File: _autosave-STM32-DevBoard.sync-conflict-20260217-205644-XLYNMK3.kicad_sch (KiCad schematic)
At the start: 55 parts, among them J1 I2C Bus 1, J2 Serial Debugger, J3 USART1, J4 12402012E212A, J5 PJ-002A, Q1 AO3401A, SW1 SW_SPDT, U1 STM32F103C8T6, U2 TPS563209DDCR, U3 USBLC6-2SC6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

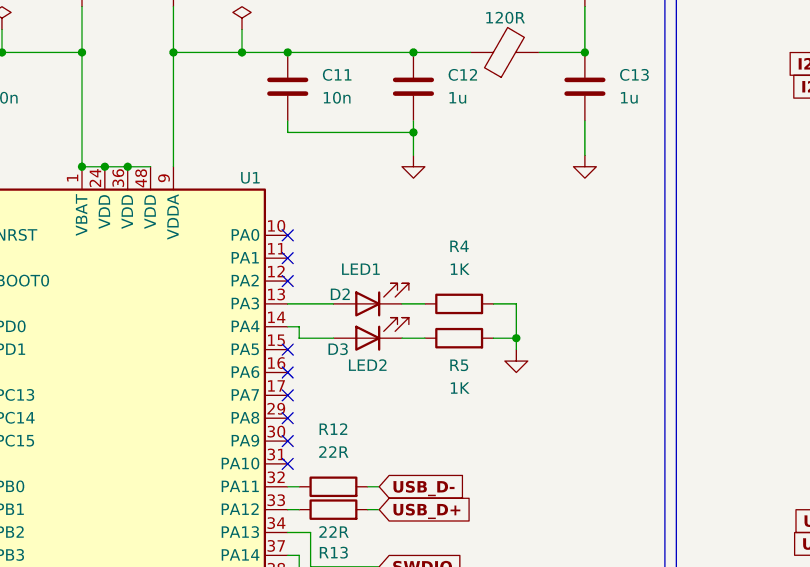
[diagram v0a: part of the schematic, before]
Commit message: Schematic complete, preliminary pcb layout done
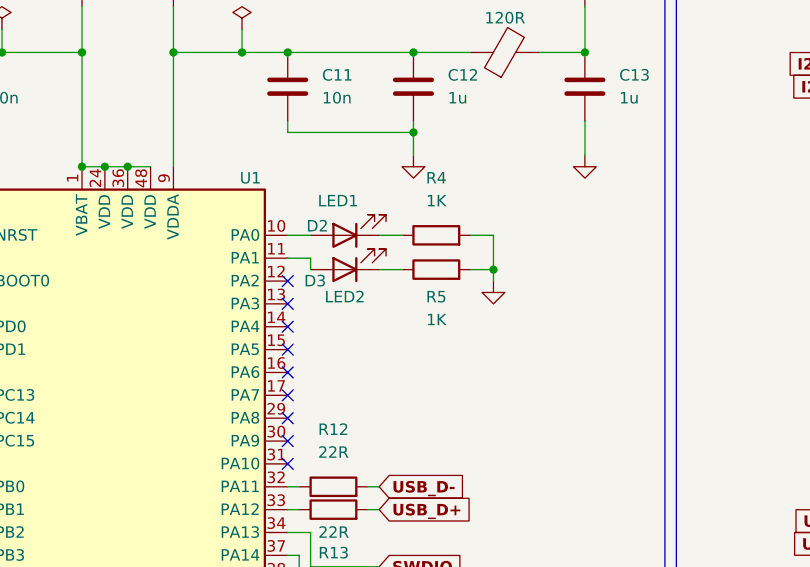
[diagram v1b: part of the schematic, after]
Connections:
- net at D3.2 (A): now also U1.11 (PA1); no longer U1.14 (PA4)
- net at U1.10 (PA0): now also D2.2 (A)
- net at U1.13 (PA3): no longer D2.2 (A)
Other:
- moved on the sheet: D2, D3, R4, R5
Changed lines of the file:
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@@
 	)
 	(junction
-		(at 133.35 120.65)
+		(at 130.81 113.03)
 		(diameter 0)
 		(color 0 0 0 0)
@@
 	)
 	(no_connect
-		(at 107.95 109.22)
+		(at 107.95 119.38)
 	)
 	(no_connect
@@
 	)
 	(no_connect
+		(at 107.95 116.84)
+	)
+	(no_connect
 		(at 72.39 129.54)
 	)
@@
 		(at 72.39 167.64)
 	)
-	(no_connect
-		(at 107.95 111.76)
-	)
 	(wire
 		(pts
@@
 	(wire
 		(pts
-			(xy 109.22 119.38) (xy 109.22 120.65)
+			(xy 46.99 96.52) (xy 46.99 97.79)
 		)
 		(stroke
@@
 	(wire
 		(pts
-			(xy 46.99 96.52) (xy 46.99 97.79)
+			(xy 215.9 132.08) (xy 218.44 132.08)
 		)
 		(stroke
@@
 	(wire
 		(pts
-			(xy 215.9 132.08) (xy 218.44 132.08)
+			(xy 128.27 109.22) (xy 130.81 109.22)
 		)
 		(stroke
@@
 	(wire
 		(pts
-			(xy 130.81 116.84) (xy 133.35 116.84)
+			(xy 110.49 111.76) (xy 110.49 113.03)
 		)
 		(stroke
@@
 	(wire
 		(pts
-			(xy 133.35 116.84) (xy 133.35 120.65)
+			(xy 130.81 109.22) (xy 130.81 113.03)
 		)
 		(stroke
@@
 	(wire
 		(pts
-			(xy 130.81 120.65) (xy 133.35 120.65)
+			(xy 128.27 113.03) (xy 130.81 113.03)
 		)
 		(stroke
@@
 	(wire
 		(pts
-			(xy 109.22 120.65) (xy 113.03 120.65)
+			(xy 107.95 111.76) (xy 110.49 111.76)
 		)
 		(stroke
@@
 	(wire
 		(pts
+			(xy 107.95 109.22) (xy 110.49 109.22)
+		)
+		(stroke
+			(width 0)
+			(type default)
+		)
+	)
+	(wire
+		(pts
 			(xy 182.88 138.43) (xy 177.8 138.43)
 		)
@@
 	(wire
 		(pts
-			(xy 107.95 116.84) (xy 113.03 116.84)
-		)
-		(stroke
-			(width 0)
-			(type default)
-		)
-	)
-	(wire
-		(pts
 			(xy 110.49 146.05) (xy 110.49 142.24)
 		)
@@
 	(wire
 		(pts
-			(xy 120.65 116.84) (xy 123.19 116.84)
+			(xy 118.11 109.22) (xy 120.65 109.22)
 		)
 		(stroke
@@
 	(wire
 		(pts
-			(xy 107.95 119.38) (xy 109.22 119.38)
-		)
-		(stroke
-			(width 0)
-			(type default)
-		)
-	)
-	(wire
-		(pts
 			(xy 99.06 44.45) (xy 99.06 54.61)
 		)
@@
 	(wire
 		(pts
-			(xy 133.35 120.65) (xy 133.35 121.92)
+			(xy 130.81 113.03) (xy 130.81 114.3)
 		)
 		(stroke
@@
 	(wire
 		(pts
-			(xy 120.65 120.65) (xy 123.19 120.65)
+			(xy 118.11 113.03) (xy 120.65 113.03)
 		)
 		(stroke
@@
 	(symbol
 		(lib_id "Device:R")
-		(at 127 116.84 90)
+		(at 124.46 109.22 90)
 		(unit 1)
 		(exclude_from_sim no)
@@
 		(fields_autoplaced yes)
 		(property "Reference" "R4"
-			(at 127 110.49 90)
+			(at 124.46 102.87 90)
 			(effects
 				(font
@@
 		)
 		(property "Value" "1K"
-			(at 127 113.03 90)
+			(at 124.46 105.41 90)
 			(effects
 				(font
@@
 		)
 		(property "Footprint" "Resistor_SMD:R_0402_1005Metric"
-			(at 127 118.618 90)
+			(at 124.46 110.998 90)
 			(effects
 				(font
@@
 		)
 		(property "Datasheet" "~"
-			(at 127 116.84 0)
+			(at 124.46 109.22 0)
 			(effects
 				(font
@@
 		)
 		(property "Description" "Resistor"
-			(at 127 116.84 0)
+			(at 124.46 109.22 0)
 			(effects
 				(font
@@
 	(symbol
 		(lib_id "power:GND")
-		(at 133.35 121.92 0)
+		(at 130.81 114.3 0)
 		(unit 1)
 		(exclude_from_sim no)
@@
 		(fields_autoplaced yes)
 		(property "Reference" "#PWR015"
-			(at 133.35 128.27 0)
+			(at 130.81 120.65 0)
 			(effects
 				(font
@@
 		)
 		(property "Value" "GND"
-			(at 133.35 127 0)
+			(at 130.81 119.38 0)
 			(effects
 				(font
@@
 		)
 		(property "Footprint" ""
-			(at 133.35 121.92 0)
+			(at 130.81 114.3 0)
 			(effects
 				(font
@@
 		)
 		(property "Datasheet" ""
-			(at 133.35 121.92 0)
+			(at 130.81 114.3 0)
 			(effects
 				(font
@@
 		)
 		(property "Description" "Power symbol creates a global label with name \"GND\" , ground"
-			(at 133.35 121.92 0)
+			(at 130.81 114.3 0)
 			(effects
 				(font
@@
 	(symbol
 		(lib_id "Device:R")
-		(at 127 120.65 90)
+		(at 124.46 113.03 90)
 		(unit 1)
 		(exclude_from_sim no)
@@
 		(dnp no)
 		(property "Reference" "R5"
-			(at 127 123.698 90)
+			(at 124.46 116.078 90)
 			(effects
 				(font
@@
 		)
 		(property "Value" "1K"
-			(at 127 126.238 90)
+			(at 124.46 118.618 90)
 			(effects
 				(font
@@
 		)
 		(property "Footprint" "Resistor_SMD:R_0402_1005Metric"
-			(at 127 122.428 90)
+			(at 124.46 114.808 90)
 			(effects
 				(font
@@
 		)
 		(property "Datasheet" "~"
-			(at 127 120.65 0)
+			(at 124.46 113.03 0)
 			(effects
 				(font
@@
 		)
 		(property "Description" "Resistor"
-			(at 127 120.65 0)
+			(at 124.46 113.03 0)
 			(effects
 				(font
@@
 	(symbol
 		(lib_id "Device:LED")
-		(at 116.84 120.65 180)
+		(at 114.3 113.03 180)
 		(unit 1)
 		(exclude_from_sim no)
@@
 		(dnp no)
 		(property "Reference" "D3"
-			(at 113.538 121.92 0)
+			(at 110.998 114.3 0)
 			(effects
 				(font
@@
 		)
 		(property "Value" "LED2"
-			(at 116.84 123.698 0)
+			(at 114.3 116.078 0)
 			(effects
 				(font
@@
 		)
 		(property "Footprint" "LED_SMD:LED_0603_1608Metric"
-			(at 116.84 120.65 0)
+			(at 114.3 113.03 0)
 			(effects
 				(font
@@
 		)
 		(property "Datasheet" "~"
-			(at 116.84 120.65 0)
+			(at 114.3 113.03 0)
 			(effects
 				(font
@@
 		)
 		(property "Description" "Light emitting diode"
-			(at 116.84 120.65 0)
+			(at 114.3 113.03 0)
 			(effects
 				(font
@@
 		)
 		(property "Sim.Pins" "1=K 2=A"
-			(at 116.84 120.65 0)
+			(at 114.3 113.03 0)
 			(effects
 				(font
@@
 	(symbol
 		(lib_id "Device:LED")
-		(at 116.84 116.84 180)
+		(at 114.3 109.22 180)
 		(unit 1)
 		(exclude_from_sim no)
@@
 		(dnp no)
 		(property "Reference" "D2"
-			(at 113.792 115.824 0)
+			(at 111.252 108.204 0)
 			(effects
 				(font
@@
 		)
 		(property "Value" "LED1"
-			(at 116.078 113.03 0)
+			(at 113.538 105.41 0)
 			(effects
 				(font
@@
 		)
 		(property "Footprint" "LED_SMD:LED_0603_1608Metric"
-			(at 116.84 116.84 0)
+			(at 114.3 109.22 0)
 			(effects
 				(font
@@
 		)
 		(property "Datasheet" "~"
-			(at 116.84 116.84 0)
+			(at 114.3 109.22 0)
 			(effects
 				(font
@@
 		)
 		(property "Description" "Light emitting diode"
-			(at 116.84 116.84 0)
+			(at 114.3 109.22 0)
 			(effects
 				(font
@@
 		)
 		(property "Sim.Pins" "1=K 2=A"
-			(at 116.84 116.84 0)
+			(at 114.3 109.22 0)
 			(effects
 				(font
